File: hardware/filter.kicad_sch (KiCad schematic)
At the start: 55 parts, among them J2 Pots Main, J3 Pots Front, Q1 KSC1815, Q2 KSC1815, U4 NJM4558D, U5 NJM4558D

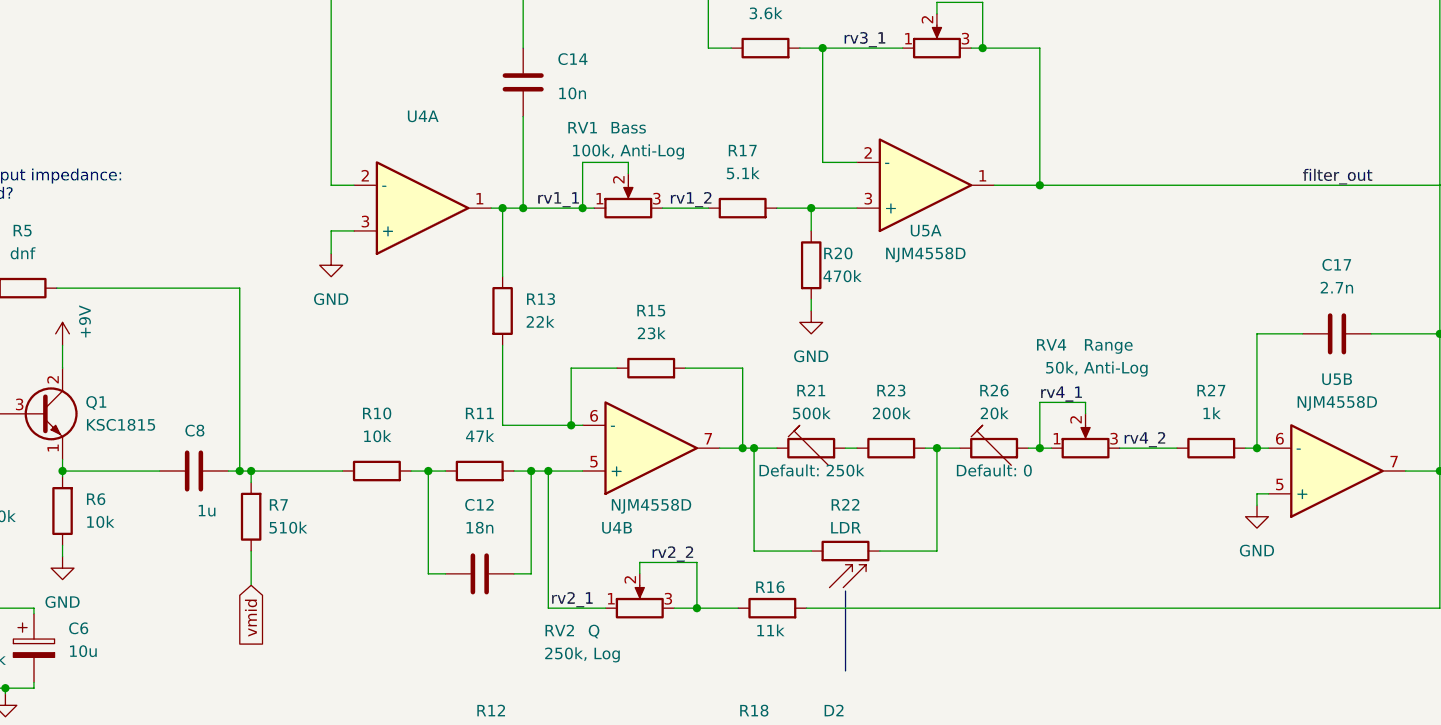
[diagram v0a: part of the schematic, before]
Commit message: Fix integrator positive input (is now vmid)
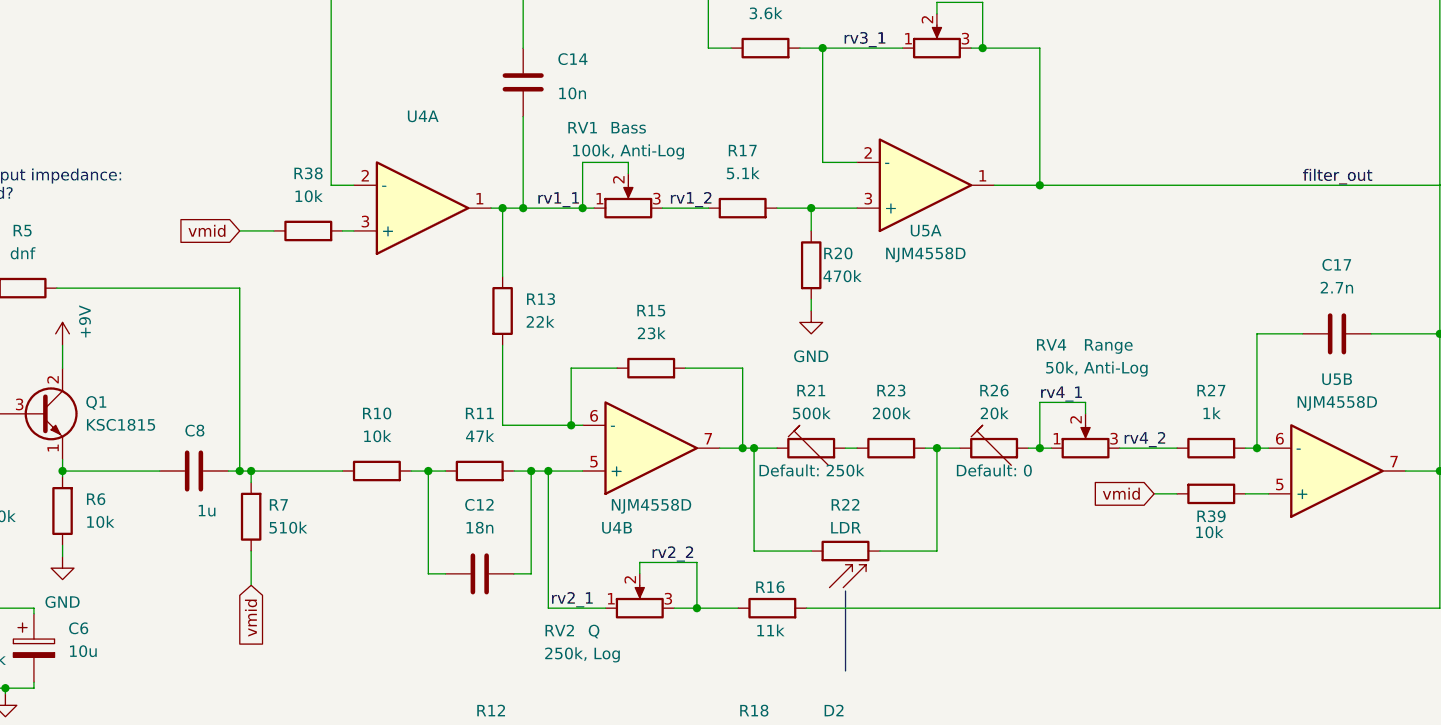
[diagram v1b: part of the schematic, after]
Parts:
- added R38, R39: 10k, Resistor_SMD:R_0805_2012Metric_Pad1.20x1.40mm_HandSolder, symbol Device:R
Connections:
- net GND: no longer U4.3 (+), U5.5 (+)
- net vmid: now also R38.1, R39.2
- new net: R38.2, U4.3 (+)
- new net: R39.1, U5.5 (+)

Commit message: Fix unintended filter_out signal union. Revise some placement.
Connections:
- net filter_out: no longer C20.1, J2.9 (Pin_9), J3.9 (Pin_9), R33.2, RV3.2, RV3.3, U5.1
- new net rv3_3: C20.1, J2.9 (Pin_9), J3.9 (Pin_9), R33.2, RV3.2, RV3.3, U5.1
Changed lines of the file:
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@@
-		)
-	)
-	(label "filter_out"
-		(at 195.58 63.5 0)
-		(fields_autoplaced yes)
-		(effects
-			(font
-				(size 1.27 1.27)
-			)
-			(justify left bottom)
 		)
 	)
@@
 		)
 	)
-	(label "filter_out"
+	(label "rv3_3"
+		(at 162.56 48.26 0)
+		(fields_autoplaced yes)
+		(effects
+			(font
+				(size 1.27 1.27)
+			)
+			(justify left bottom)
+		)
+	)
+	(label "rv3_3"
 		(at 228.6 133.985 0)
 		(fields_autoplaced yes)

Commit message: Change R20 value to 4k7
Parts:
- R20: value 470k -> 4.7k
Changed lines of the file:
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@@
 			)
 		)
-		(property "Value" "470k"
+		(property "Value" "4.7k"
 			(at 142.24 73.66 0)
 			(effects

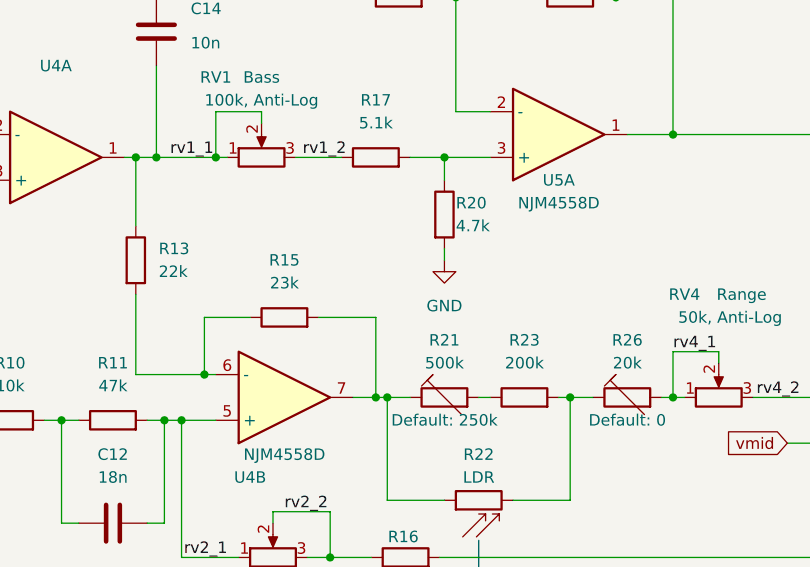
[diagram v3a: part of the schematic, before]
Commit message: Fix: Connect R20 low side to Vmid instead of GND
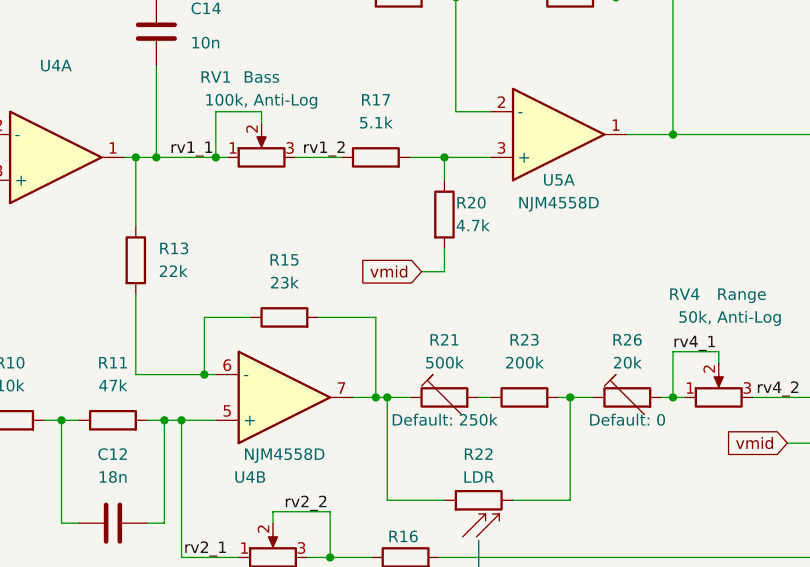
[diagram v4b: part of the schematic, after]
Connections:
- net GND: no longer R20.2
- net vmid: now also R20.2
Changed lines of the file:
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@@
 	(wire
 		(pts
+			(xy 138.43 78.74) (xy 140.97 78.74)
+		)
+		(stroke
+			(width 0)
+			(type default)
+		)
+	)
+	(wire
+		(pts
 			(xy 147.32 128.27) (xy 153.67 128.27)
 		)
@@
 	(wire
 		(pts
-			(xy 140.97 76.2) (xy 140.97 77.47)
+			(xy 140.97 76.2) (xy 140.97 78.74)
 		)
 		(stroke
@@
 	(global_label "vmid"
 		(shape input)
+		(at 138.43 78.74 180)
+		(fields_autoplaced yes)
+		(effects
+			(font
+				(size 1.27 1.27)
+			)
+			(justify right)
+		)
+		(property "Intersheetrefs" "${INTERSHEET_REFS}"
+			(at 131.0301 78.74 0)
+			(effects
+				(font
+					(size 1.27 1.27)
+				)
+				(justify right)
+				(hide yes)
+			)
+		)
+	)
+	(global_label "vmid"
+		(shape input)
 		(at 224.79 74.93 270)
 		(fields_autoplaced yes)
@@
 					(unit 1)
 				)
-			)
-		)
-	)
-	(symbol
-		(lib_id "power:GND")
-		(at 140.97 77.47 0)
-		(unit 1)
-		(exclude_from_sim no)
-		(in_bom yes)
-		(on_board yes)
-		(dnp no)
-		(fields_autoplaced yes)
-		(property "Reference" "#PWR011"
-			(at 140.97 83.82 0)
-			(effects
-				(font
-					(size 1.27 1.27)
-				)
-				(hide yes)
-			)
-		)
-		(property "Value" "GND"
-			(at 140.97 82.55 0)
-			(effects
-				(font
-					(size 1.27 1.27)
-				)
-			)
-		)
-		(property "Footprint" ""
-			(at 140.97 77.47 0)
-			(effects
-				(font
-					(size 1.27 1.27)
-				)
-				(hide yes)
-			)
-		)
-		(property "Datasheet" ""
-			(at 140.97 77.47 0)
-			(effects
-				(font
-					(size 1.27 1.27)
-				)
-				(hide yes)
-			)
-		)
-		(property "Description" ""
-			(at 140.97 77.47 0)
-			(effects
-				(font
-					(size 1.27 1.27)
-				)
-				(hide yes)
-			)
-		)
-		(pin "1"
-		)
-		(instances
-			(project "umidi-wah"
-				(path "/8f66db7e-cf06-4b3a-905e-a75646e85499/159ecef9-3b03-4128-8fe9-708b096478c0"
-					(reference "#PWR011")
-					(unit 1)
-				)

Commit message: Move filter circuit to the left as far as possible
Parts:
- C12, C17: footprint Capacitor_THT:C_Rect_L7.0mm_W3.5mm_P2.50mm_P5.00mm -> Capacitor_THT:C_Rect_L7.0mm_W2.5mm_P5.00mm
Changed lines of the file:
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@@
 			)
 		)
-		(property "Footprint" "Capacitor_THT:C_Rect_L7.0mm_W3.5mm_P2.50mm_P5.00mm"
+		(property "Footprint" "Capacitor_THT:C_Rect_L7.0mm_W2.5mm_P5.00mm"
 			(at 107.95 105.7148 0)
 			(effects
@@
 			)
 		)
-		(property "Footprint" "Capacitor_THT:C_Rect_L7.0mm_W3.5mm_P2.50mm_P5.00mm"
+		(property "Footprint" "Capacitor_THT:C_Rect_L7.0mm_W2.5mm_P5.00mm"
 			(at 203.2 79.0448 0)
 			(effects

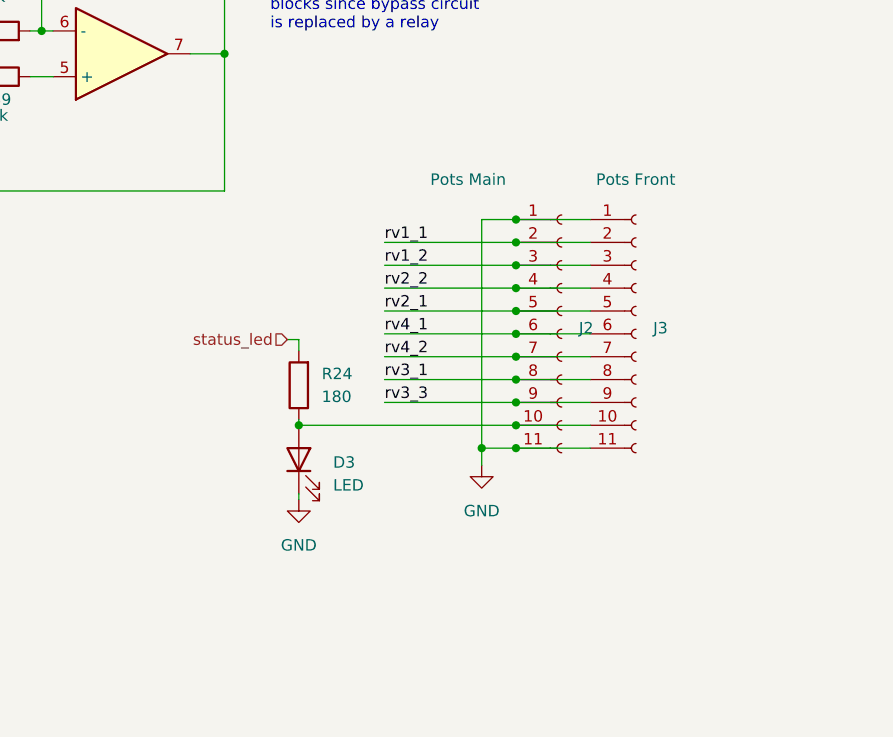
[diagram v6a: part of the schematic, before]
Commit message: Almost finish routing
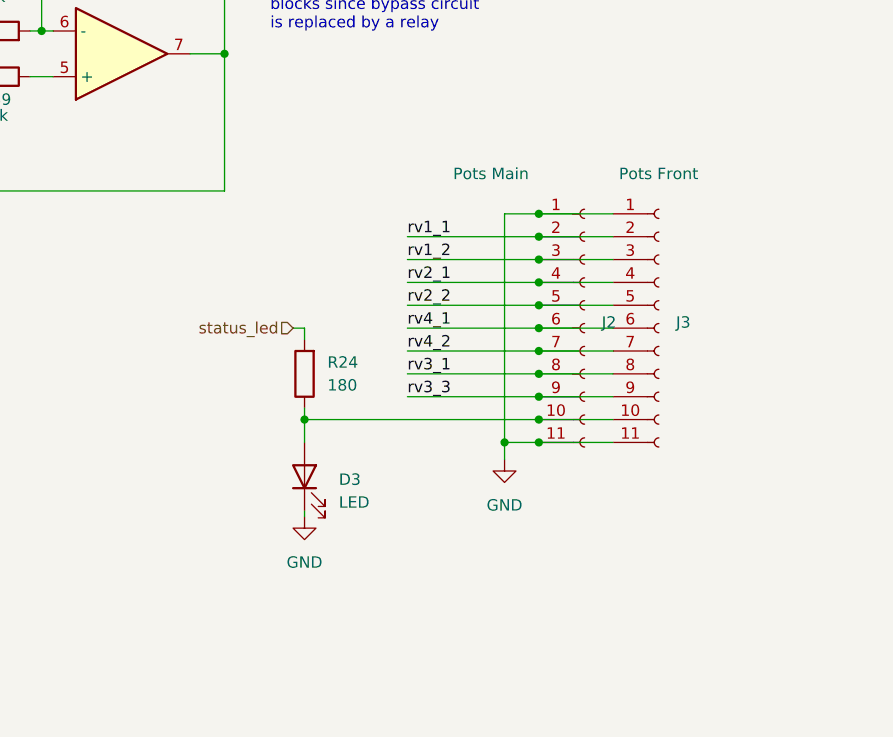
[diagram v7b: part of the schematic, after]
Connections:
- net rv2_1: now also J2.4 (Pin_4), J3.4 (Pin_4); no longer J2.5 (Pin_5), J3.5 (Pin_5)
- net rv2_2: now also J2.5 (Pin_5), J3.5 (Pin_5); no longer J2.4 (Pin_4), J3.4 (Pin_4)
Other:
- moved on the sheet: D3, J2, J3, R24

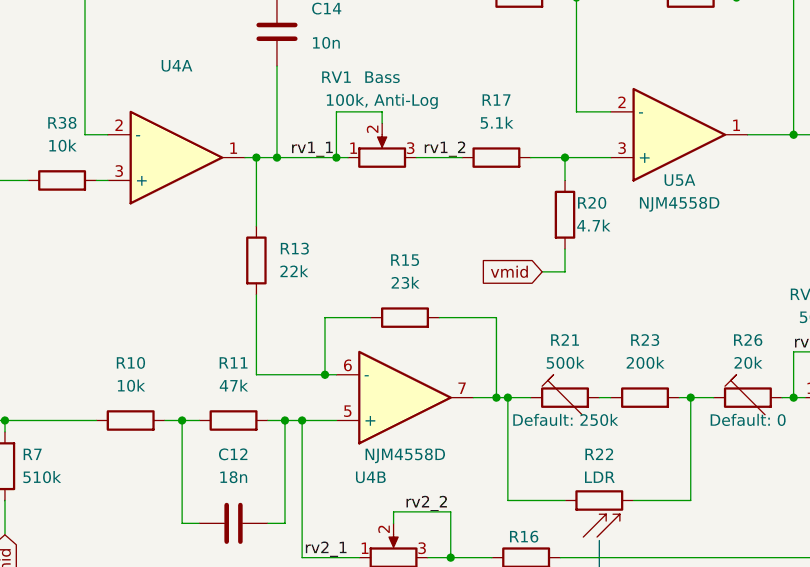
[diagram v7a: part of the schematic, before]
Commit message: Update to KiCAD 10; Set R15 from 23k to 23k2 (E96)
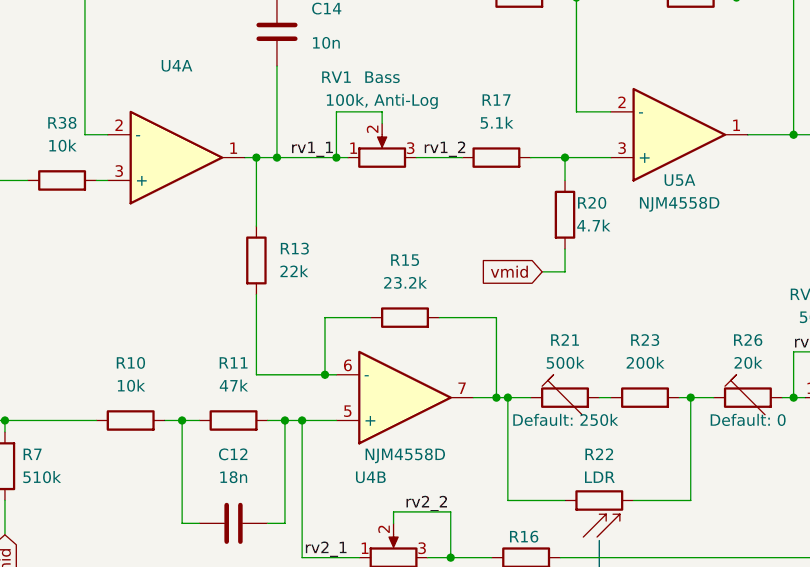
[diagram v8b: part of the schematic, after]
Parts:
- R15: value 23k -> 23.2k
